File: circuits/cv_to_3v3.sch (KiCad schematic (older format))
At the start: 17 parts, among them U6 MCP6009

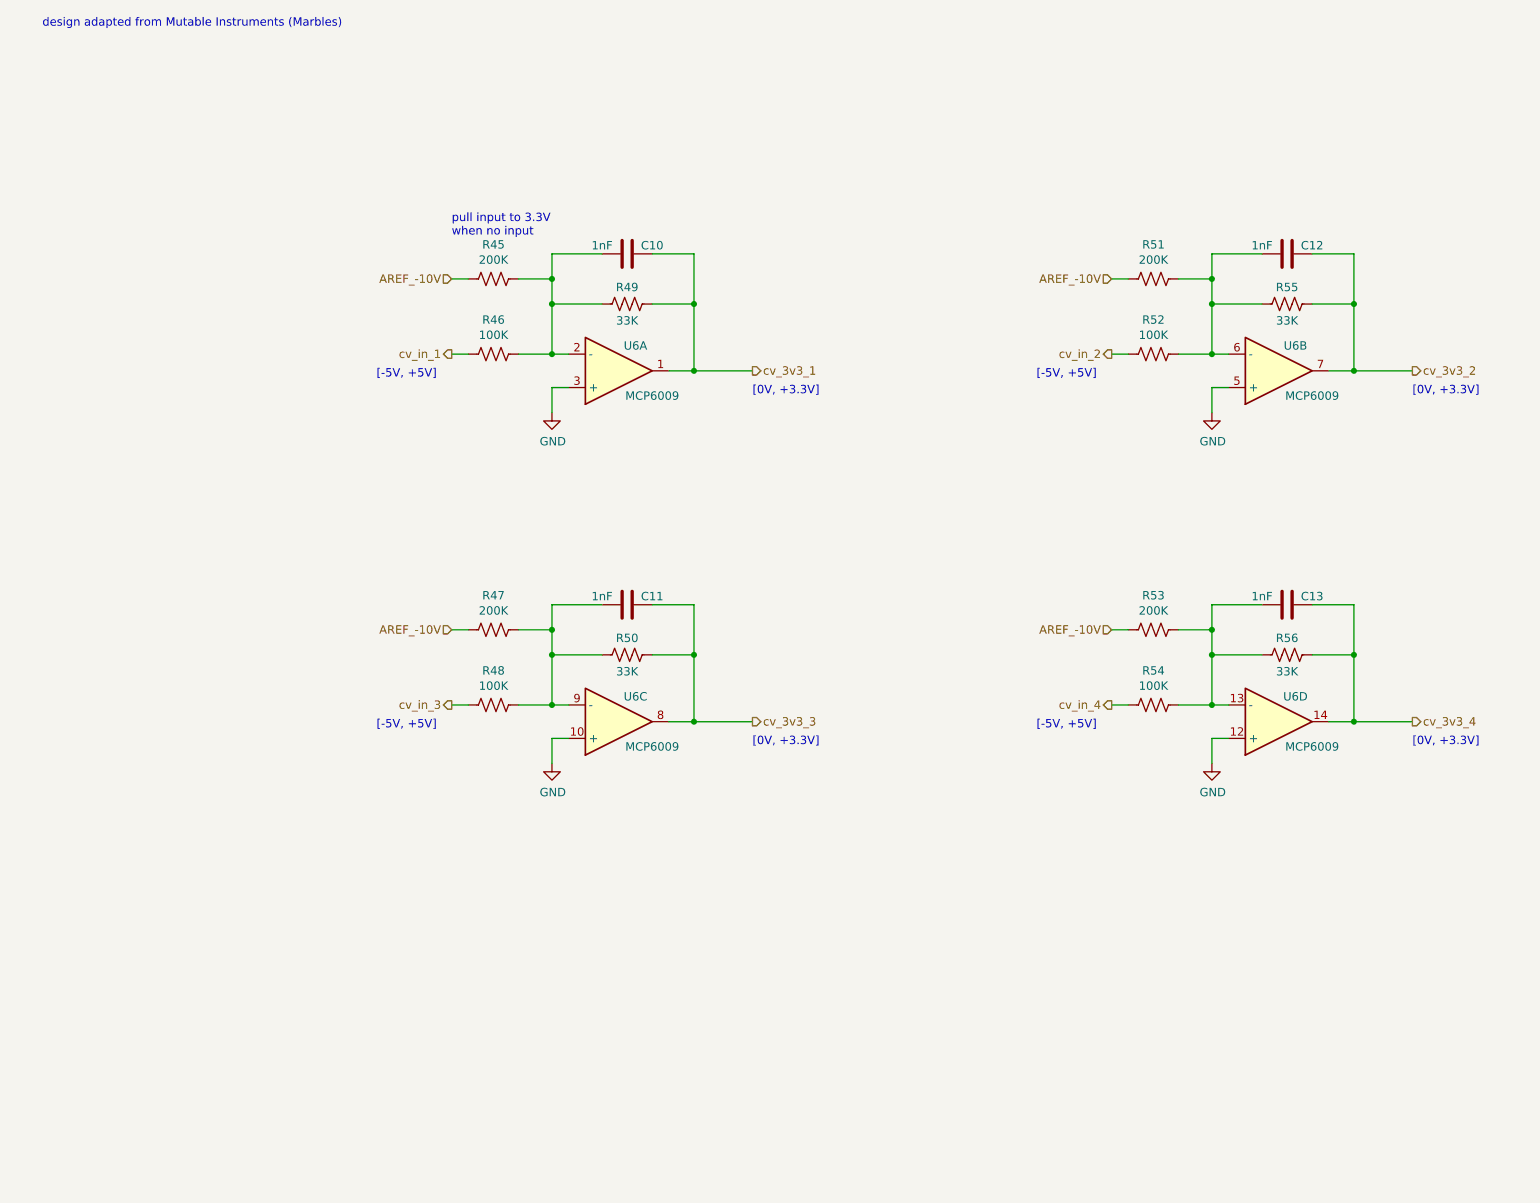
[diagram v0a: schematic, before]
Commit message: updating circuit fragements with simulation links and fixing bugs
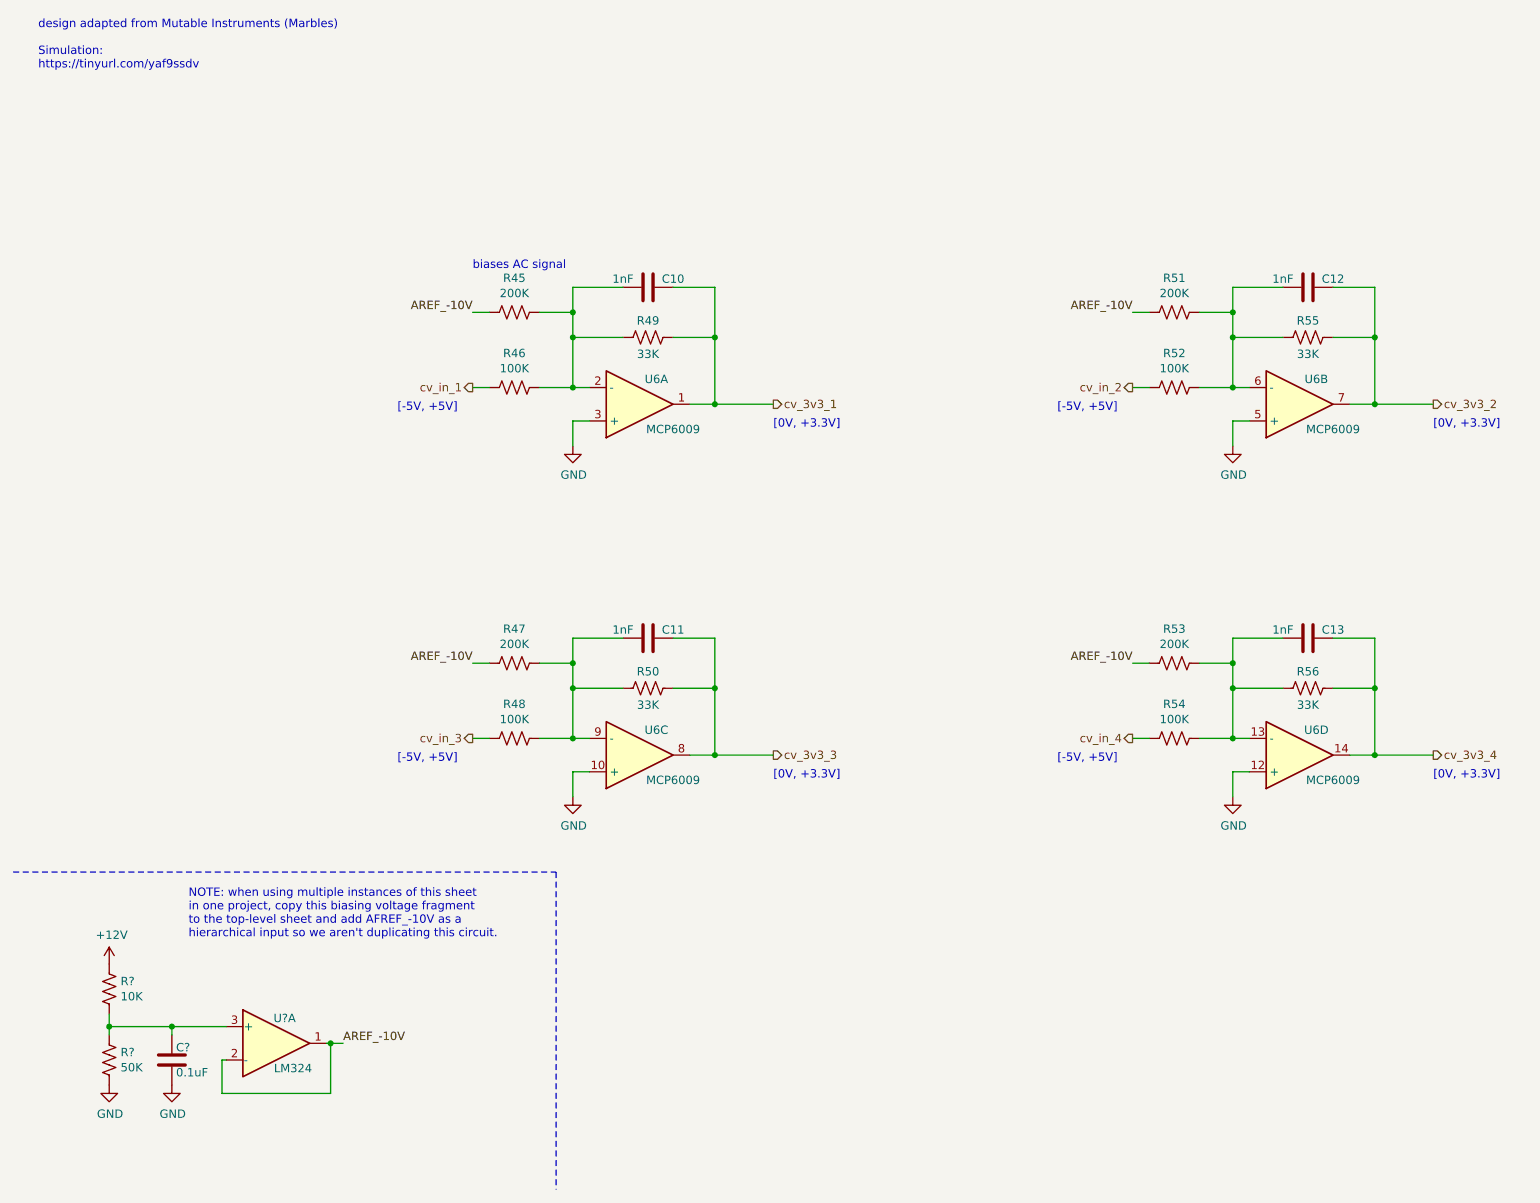
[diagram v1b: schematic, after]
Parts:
- added C?: 0.1uF, symbol Device:C
- added R?: 10K, symbol Device:R_US
- added R?: 50K, symbol Device:R_US
- added U?: LM324, symbol Amplifier_Operational:LM324
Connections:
- net AREF_-10V: now also U?.1, U?.2 (-)
- net GND: now also C?.2, R?.2
- new net: C?.1, R?.1, R?.2, U?.3 (+)
- new net +12V: R?.1
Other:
- note added: "NOTE: when using multiple instances of this sheet\nin one project, copy this biasing voltage fragment\nto the top-level sheet and add AFREF_-10V as a\nhierarchical input so we aren't duplicating this circuit."
- note added: "biases AC signal"
- note added: "design adapted from Mutable Instruments (Marbles)\n\nSimulation:\nhttps://tinyurl.com/yaf9ssdv"
- note removed: "design adapted from Mutable Instruments (Marbles)"
- note removed: "pull input to 3.3V\nwhen no input"
- moved on the sheet: C10, C11, C12, C13, R45, R46, R47, R48, R49, R50, R51, R52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
